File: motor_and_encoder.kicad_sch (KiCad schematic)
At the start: 6 parts, among them J5_1 Conn_02x03_Odd_Even, J5_2 Conn_02x03_Odd_Even, U5_1 DRV8835DSSR

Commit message: DRV8835のシンボルのピン割当ミスを修正してシンボル回路図修正(6->8)
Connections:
- net MOTOR2_PHASE: now also U5_1.8 (BIN1/B_PHASE); no longer U5_1.6 (GND)
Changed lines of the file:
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@@
     (pin "5")
     (pin "6")
-    (pin "6")
     (pin "7")
+    (pin "8")
     (pin "9")
     (instances

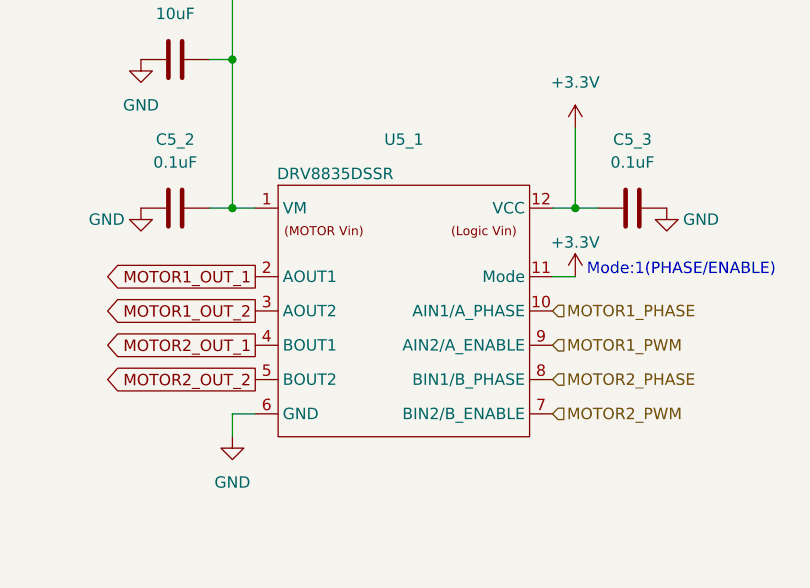
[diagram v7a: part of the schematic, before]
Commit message: DRV8835用にフットプリント作ってシンボルと紐付けた（シンボルも少し更新）
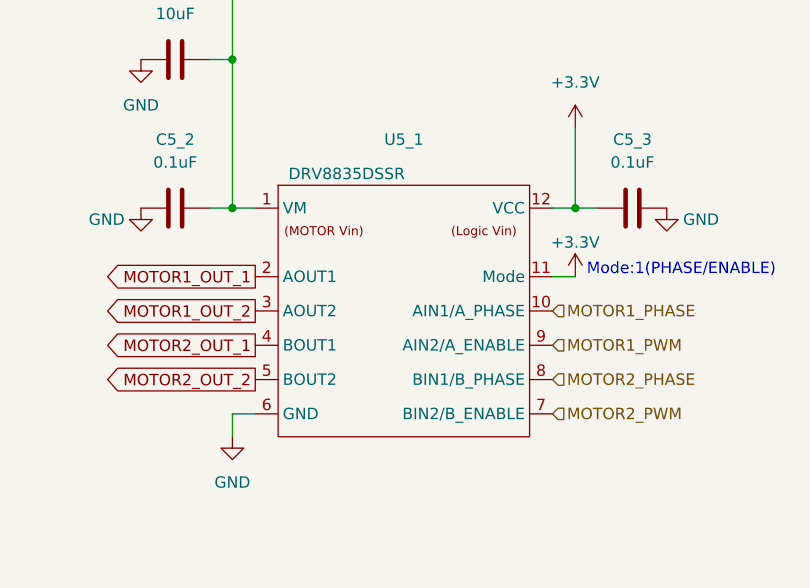
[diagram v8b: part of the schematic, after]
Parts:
- U5_1: footprint Self-Made_Generic_Packages:WSON-12-1EP_ExpandPad_3x2mm_P0.5mm_EP1x2.65 -> DRV8835:DRV8835_ThermalExpanded_WSON-12-1EP
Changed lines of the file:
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@@
     )
   )
-  (symbol (lib_id "DRV8835:DRV8835") (at 148.59 87.63 0) (unit 1)
+  (symbol (lib_id "DRV8835:DRV8835") (at 175.26 77.47 0) (unit 1)
     (in_bom yes) (on_board yes) (dnp no)
     (property "Reference" "U5_1" (at 175.26 76.2 0)
       (effects (font (size 1.27 1.27)))
     )
-    (property "Value" "DRV8835DSSR" (at 167.64 80.01 0)
+    (property "Value" "DRV8835DSSR" (at 168.91 80.01 0)
       (effects (font (size 1.27 1.27)))
     )
-    (property "Footprint" "Self-Made_Generic_Packages:WSON-12-1EP_ExpandPad_3x2mm_P0.5mm_EP1x2.65" (at 148.59 87.63 0)
+    (property "Footprint" "DRV8835:DRV8835_ThermalExpanded_WSON-12-1EP" (at 175.26 77.47 0)
       (effects (font (size 1.27 1.27)) hide)
     )
-    (property "Datasheet" "" (at 148.59 87.63 0)
+    (property "Datasheet" "" (at 175.26 77.47 0)
       (effects (font (size 1.27 1.27)) hide)
     )
